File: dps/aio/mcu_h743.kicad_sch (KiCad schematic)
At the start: 65 parts, among them J301 TYPE-C 16P QTWT, J302 TF-021B-H265, J303 GPS WS-M181, J304 MTF-02P, U301 STM32H743VIH6, U302 SPL06-001 / DPS310, U303 BMI088, Y301 8MHz 12pF X32258MOB4SI

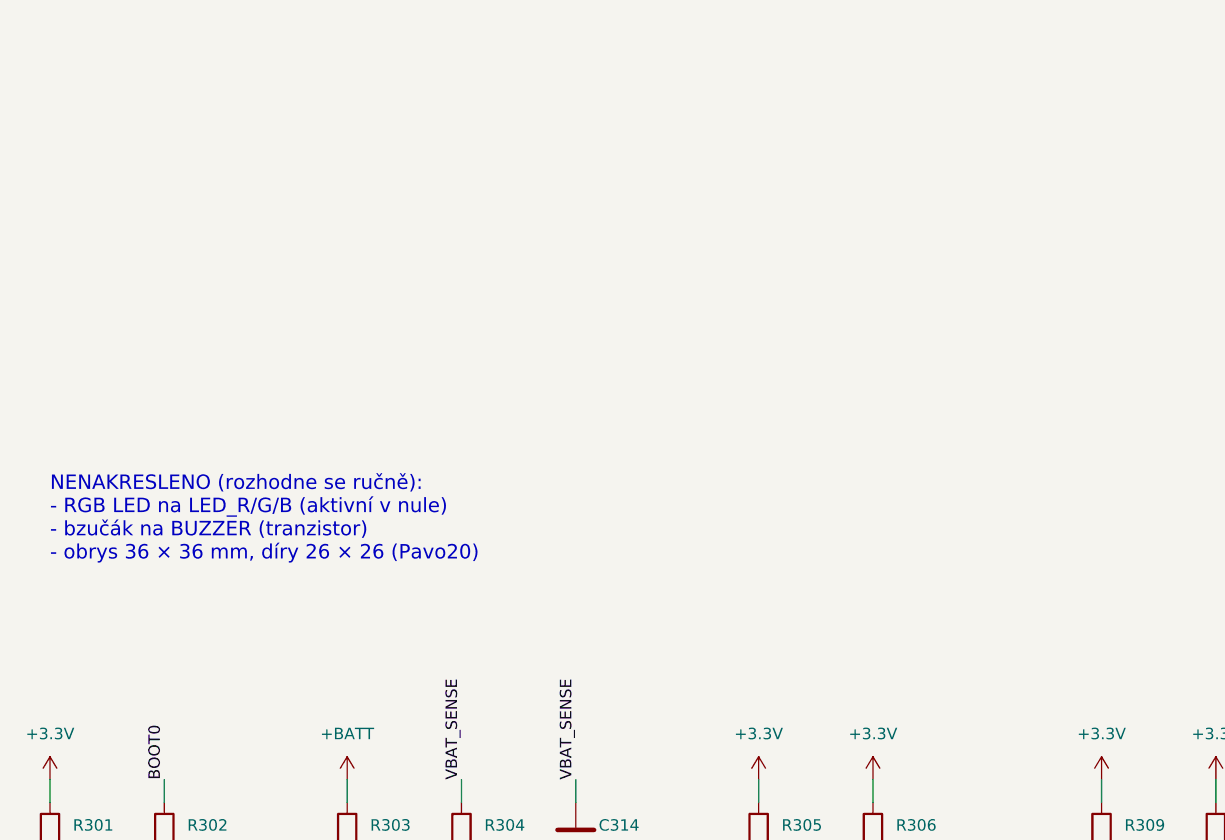
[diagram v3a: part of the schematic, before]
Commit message: feat: draw the AIO's RGB LED and buzzer switch, and keep the schematic generator in the repo
- D301-D303 XINGLIGHT XL-1005 0402 with anodes on 3.3 V: ArduPilot's
  GPIO_LED_RGB lights with a low (HAL_GPIO_LED_ON 0). Green and blue are
  OpenAIO's parts, red C965790 from the same series; 330R/150R/75R, ~3-5 mA.
- Q301 AO3400A low-side switch for an external active 5 V buzzer on pads
  BZ+/BZ- (BUZZ_ON_LVL 1), R319 holds it off through reset, D304 1N4148WS
  across the buzzer. A 2N7002 (Vgs(th) up to 2.5 V) would barely open at 3.3 V.
- dps/aio/gen/gen_aio.py writes every sheet with stable UUIDs; it now finds
  OpenAIO and KiCad's symbols on its own and only copies the board, rules,
  project and footprints when they are missing.
- NAVRH, README, web texts and tables follow; ERC still 18, explained.

Co-Authored-By: Claude Opus 5.5 <noreply@anthropic.com>
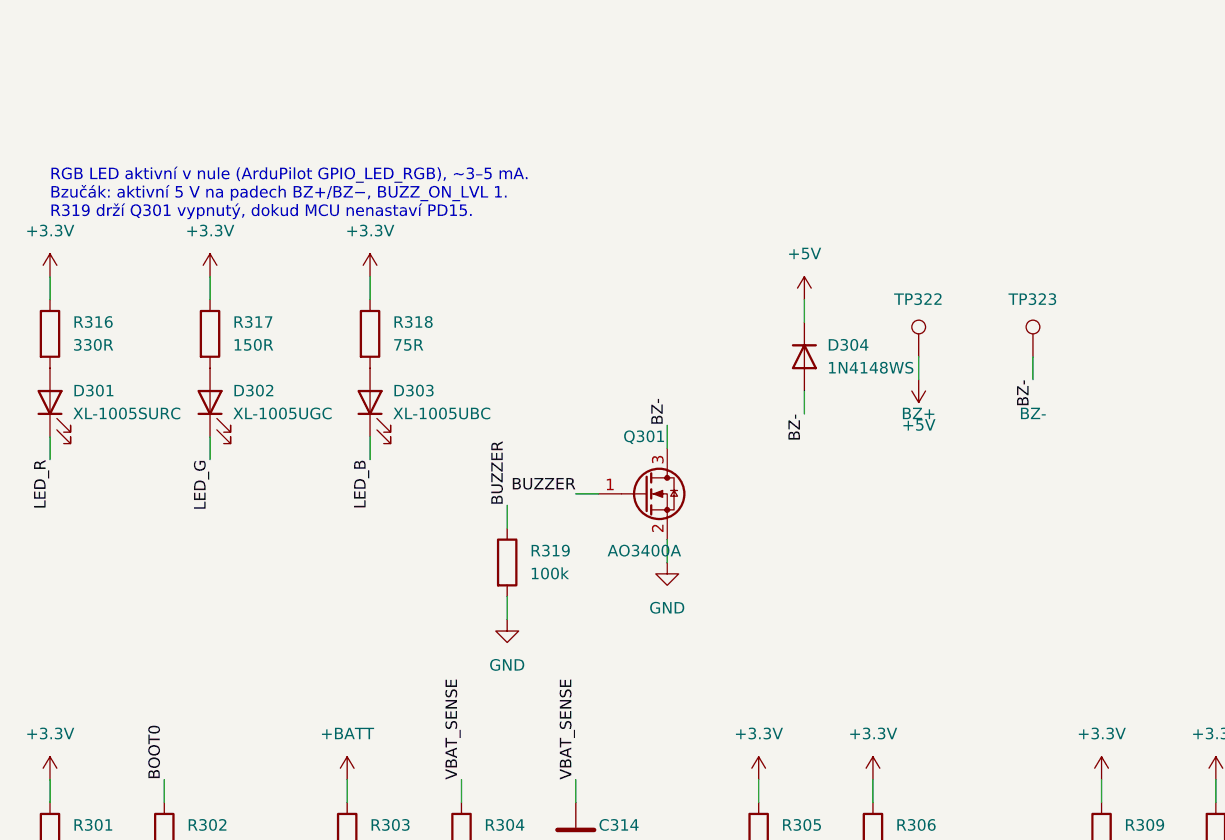
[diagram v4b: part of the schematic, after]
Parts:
- added D301: XL-1005SURC, lib:LED_0402_1005Metric, symbol lib:LED
- added D302: XL-1005UGC, lib:LED_0402_1005Metric, symbol lib:LED
- added D303: XL-1005UBC, lib:LED_0402_1005Metric, symbol lib:LED
- added D304: 1N4148WS, Diode_SMD:D_SOD-323, symbol Device:D
- added Q301: AO3400A, Package_TO_SOT_SMD:SOT-23, symbol Transistor_FET:Q_NMOS_GSD
- added R316: 330R, lib:R_0201_0603Metric, symbol lib:R
- added R317: 150R, lib:R_0201_0603Metric, symbol lib:R
- added R318: 75R, lib:R_0201_0603Metric, symbol lib:R
- added R319: 100k, lib:R_0201_0603Metric, symbol lib:R
- added TP322: BZ+, lib:TestPoint_Pad_D1.0mm, symbol lib:TestPoint
- added TP323: BZ-, lib:TestPoint_Pad_D1.0mm, symbol lib:TestPoint
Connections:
- net +3.3V: now also R316.1, R317.1, R318.1
- net +5V: now also D304.1 (K), TP322.1
- net BUZZER: now also Q301.1 (G), R319.1
- net GND: now also Q301.2 (S), R319.2
- net LED_B: now also D303.1 (K)
- net LED_G: now also D302.1 (K)
- net LED_R: now also D301.1 (K)
- new net: D303.2 (A), R318.2
- new net: D301.2 (A), R316.2
- new net: D302.2 (A), R317.2
- new net BZ-: D304.2 (A), Q301.3 (D), TP323.1
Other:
- note added: "RGB LED aktivní v nule (ArduPilot GPIO_LED_RGB), ~3–5 mA. Bzučák: aktivní 5 V na padech BZ+/BZ−, BUZZ_ON_LVL 1. R319 drží Q301 vypnutý, dokud MCU nenastaví PD15."
- note removed: "NENAKRESLENO (rozhodne se ručně): - RGB LED na LED_R/G/B (aktivní v nule) - bzučák na BUZZER (tranzistor) - obrys 36 × 36 mm, díry 26 × 26 (Pavo20)"

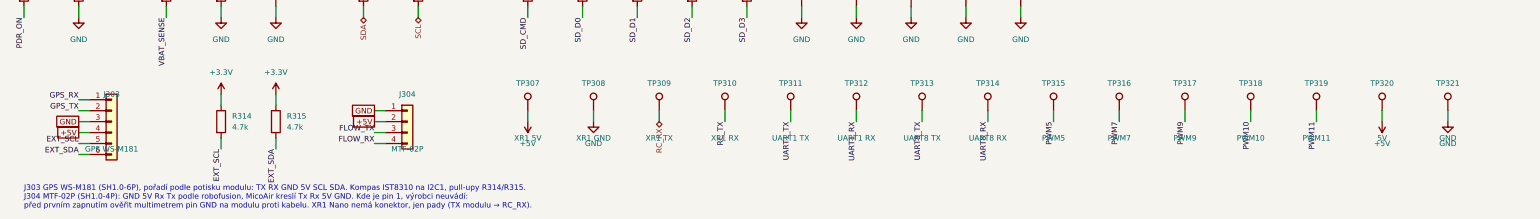
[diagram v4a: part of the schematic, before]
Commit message: feat: give the AIO MicoAir743-AIO's peripheral connectors
- J303 GPS (UART3 + I2C1), J304 UART4 and new J305 UART1 + UART6, SH1.0
  side entry, in MicoAir's order with pin 1 = GND (ArduPilot's README for the
  board puts pin 1 of the DJI connector at 12 V, the last row of its tables),
  so cables from a MicoAir fit. J305 replaces the XR1 and UART1 pads.
- The LD06 goes to pads (TP201 Tx, TP202 PWM, 5V/GND on TP320/TP321) as on
  MicoAir: the ZH1.5 connector needed 86 mm2 in one piece.
- Symbols and sheets now get UUIDs from their names, so adding or removing a
  part no longer shifts the others and breaks their link to the board.
- Placement: J304 fits on the back right edge as on MicoAir. J303 and J305 do
  not: every spot for a 6-pin SH (side 9.8 x 6.6 or vertical 9.8 x 5.2 mm)
  hits the ESC and power parts kept from OpenAIO, so they stay off the board.

Co-Authored-By: Claude Opus 5.5 <noreply@anthropic.com>
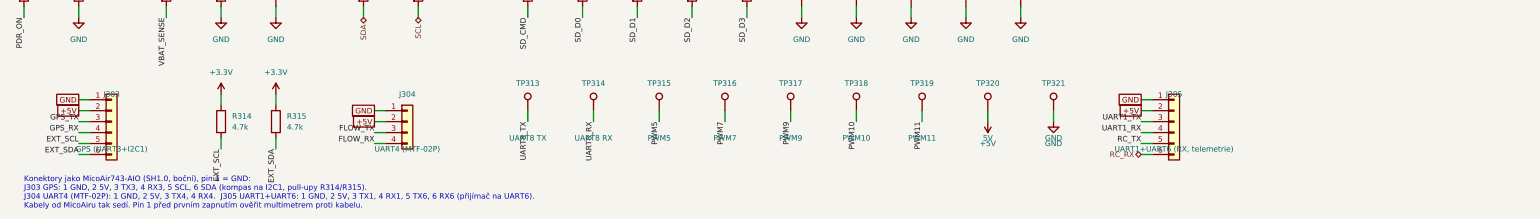
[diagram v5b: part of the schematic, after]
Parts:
- removed TP307: XR1 5V, lib:TestPoint_Pad_D1.0mm, symbol lib:TestPoint
- removed TP308: XR1 GND, lib:TestPoint_Pad_D1.0mm, symbol lib:TestPoint
- removed TP309: XR1 TX, lib:TestPoint_Pad_D1.0mm, symbol lib:TestPoint
- removed TP310: XR1 RX, lib:TestPoint_Pad_D1.0mm, symbol lib:TestPoint
- removed TP311: UART1 TX, lib:TestPoint_Pad_D1.0mm, symbol lib:TestPoint
- removed TP312: UART1 RX, lib:TestPoint_Pad_D1.0mm, symbol lib:TestPoint
- added J305: UART1+UART6 (RX, telemetrie), Connector_JST:JST_SH_SM06B-SRSS-TB_1x06-1MP_P1.00mm_Horizontal, symbol Connector_Generic:Conn_01x06
- J303: value GPS WS-M181 -> GPS (UART3+I2C1)
- J304: value MTF-02P -> UART4 (MTF-02P)
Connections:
- net +5V: now also J303.2 (Pin_2), J305.2 (Pin_2); no longer J303.4 (Pin_4)
- net GND: now also J303.1 (Pin_1), J305.1 (Pin_1); no longer J303.3 (Pin_3)
- net GPS_RX: now also J303.4 (Pin_4); no longer J303.1 (Pin_1)
- net GPS_TX: now also J303.3 (Pin_3); no longer J303.2 (Pin_2)
- net RC_RX: now also J305.6 (Pin_6)
- net RC_TX: now also J305.5 (Pin_5)
- net UART1_RX: now also J305.4 (Pin_4)
- net UART1_TX: now also J305.3 (Pin_3)
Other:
- note added: "Konektory jako MicoAir743-AIO (SH1.0, boční), pin 1 = GND: J303 GPS: 1 GND, 2 5V, 3 TX3, 4 RX3, 5 SCL, 6 SDA (kompas na I2C1, pull-upy R314/R315). J304 UART4 (MTF-02P): 1 GND, 2 5V, 3 TX4, 4 RX4. J305 UART1+UART6: 1 GND, 2 5V, 3 TX1, 4 RX1, 5 TX6, 6 RX6 (přijímač na UART6). Kabely od MicoAiru tak sedí. Pin 1 před prvním zapnutím ověřit multimetrem proti kabelu."
- note removed: "J303 GPS WS-M181 (SH1.0-6P), pořadí podle potisku modulu: TX RX GND 5V SCL SDA. Kompas IST8310 na I2C1, pull-upy R314/R315. J304 MTF-02P (SH1.0-4P): GND 5V Rx Tx podle robofusion, MicoAir kreslí Tx Rx 5V GND. Kde je pin 1, výrobci neuvádí: před prvním zapnutím ověřit multimetrem pin GND na modulu proti kabelu. XR1 Nano nemá konektor, jen pady (TX modulu → RC_RX)."

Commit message: feat: put all four MicoAir connectors on the AIO's edge and place it without the INA226
- The edge search found four spots no kept OpenAIO part blocks, so the ESCs
  stay as they are: J201 VTX front bottom, J303 GPS front right below motor 4,
  J305 UART1+UART6 back right, J304 UART4 back bottom. Motor pads are front
  only and the battery pads take the top edge, hence not MicoAir's places.
- Pads as on MicoAir: new lib:Pad_1.0x1.4mm (courtyard 1.2 x 1.6) instead of
  1 mm round test points with a 2 x 2 courtyard.
- Dropped for room, none of them on MicoAir: the VTX INA226 with its shunt,
  JP201 and the buzzer diode; Q301 is OpenAIO's AP1606 in DFN 1.0 x 0.6
  instead of an AO3400A in SOT-23. BATT2 defaults go; firmware rebuilt.
- Placement now treats pads, holes on both sides and the outer-layer copper
  of nets no new part uses (ESC inside, +BATT, the CSA+ via field) as
  obstacles, in 1 mm cells. vycisti_med.py removes the dangling RP2354
  leftovers and copper the new parts land on, never CSA+ or +BATT; the
  updater swaps changed footprints and sets sheet names.
- U303 (BMI088) and U201 (VTX buck) do not fit: no 3.3 x 3.3 mm is left on
  either side. DRC: 163 unconnected, otherwise OpenAIO's own warnings.

Co-Authored-By: Claude Opus 5.5 <noreply@anthropic.com>
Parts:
- removed D304: 1N4148WS, Diode_SMD:D_SOD-323, symbol Device:D
- Q301: value AO3400A -> AP1606; footprint Package_TO_SOT_SMD:SOT-23 -> lib:DFN-3L_L1.0-W0.6-P0.65-BR; symbol Transistor_FET:Q_NMOS_GSD -> lib:DMN1150UFB-7B; LCSC C20917 -> C2849580
- TP301, TP302, TP303, TP304, TP305, TP306, TP313, TP314, TP315, TP316, TP317, TP318, TP319, TP320, TP321, TP322, TP323: footprint lib:TestPoint_Pad_D1.0mm -> lib:Pad_1.0x1.4mm
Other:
- note added: "RGB LED aktivní v nule (ArduPilot GPIO_LED_RGB), ~3–5 mA. Bzučák: aktivní 5 V (piezo) na padech BZ+/BZ−, BUZZ_ON_LVL 1, bez diody jako MicoAir. R319 drží Q301 vypnutý, dokud MCU nenastaví PD15."
- note removed: "RGB LED aktivní v nule (ArduPilot GPIO_LED_RGB), ~3–5 mA. Bzučák: aktivní 5 V na padech BZ+/BZ−, BUZZ_ON_LVL 1. R319 drží Q301 vypnutý, dokud MCU nenastaví PD15."

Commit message: feat: fit every AIO part on the board: switch the VTX off +10V and take an ICM-42688-P as the second IMU
The VTX buck and the BMI088 did not fit; the largest free spot was 2.5 x 2.9 mm.
The VTX now hangs on fc_power's +10V behind a TPS22810 load switch (as OpenAIO
feeds it, but switchable), and the second IMU is an ICM-42688-P on OpenAIO's
LGA-14 footprint. The board update now also carries values and LCSC numbers.

Co-Authored-By: Claude Opus 5.5 <noreply@anthropic.com>
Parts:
- added C324: 10n, lib:C_0201_0603Metric, symbol lib:C
- C319: value 100n -> 2.2uF; LCSC C76939 -> (none)
- U303: value BMI088 -> ICM-42688-P; footprint Package_LGA:Bosch_LGA-16_4.5x3mm_P0.5mm_LayoutBorder7x1y_ClockwisePinNumbering -> lib:LGA-14_L3.0-W2.5-P0.50-BR; symbol Sensor_Motion:BMI088 -> lib:LSM6DSV16XTR
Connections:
- net +3.3V: now also U303.5 (Vdd_IO), U303.8 (Vdd), C324.1; no longer U303.11 (VDDIO), U303.3 (VDD)
- net GND: now also U303.10 (OCS_Aux), U303.11 (SDO_Aux), U303.3 (SCx/AH2/Qvar2), U303.9 (INT2), C324.2; no longer U303.4 (GNDA)
- net IMU2_MISO: now also U303.1 (SDO/SA0); no longer U303.10 (SDO2), U303.15 (SDO1)
- net IMU2_MOSI: now also U303.14 (SDA); no longer U303.9 (SDI/SDA)
- net IMU2_SCK: now also U303.13 (SCL); no longer U303.8 (SCK/SCL)
- net IMU2_ACC_CS renamed IMU2_CS
- net IMU2_CS: now also U303.12 (CS); no longer U303.14 (~{CSB1})
- net IMU2_ACC_INT renamed IMU2_INT
- net IMU2_INT: now also U303.4 (INT1); no longer U303.16 (INT1)
- net IMU2_GYR_CS: no longer names the net of U301.B6 (PD5)
- net IMU2_GYR_CS: no longer U303.5 (~{CSB2})
- net IMU2_GYR_INT: no longer names the net of U301.B1 (PC15)
- net IMU2_GYR_INT: no longer U303.12 (INT3)
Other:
- note added: "U303 ICM-42688-P na SPI2 (MicoAir tu má BMI088, 4,5 × 3 mm se nevešel). Pouzdro LGA-14 2,5 × 3 jako BMI270. INT1 = data ready, RESV a FSYNC na GND. VDD 100 nF + 2,2 µF (C318, C319), VDDIO 10 nF (C324) podle DS-000347."
- note removed: "U303 BMI088 jako MicoAir: SPI2, PS = GND (SPI), SDO1+SDO2 = MISO, INT1 = data ready akcel., INT3 = gyro."
- moved on the sheet: C317

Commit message: feat: route the AIO with its own router after laying it out like MicoAir
The peripherals sat where OpenAIO put them for the RP2354, so about 20 signals
left the H743's BGA on the wrong side. The connectors now sit as on MicoAir,
mirrored, and GPS, receiver, LD06 and both IMUs move to pins whose balls face
them; SERIAL_ORDER keeps the SERIALn numbers. New scripts escape the BGA, clear
OpenAIO leftovers, route in several passes, stitch GND islands and place the
USB-C D+/D- jumpers. 134 of 156 pairs are routed, 22 remain, DRC is clean.

Co-Authored-By: Claude Opus 5.5 <noreply@anthropic.com>
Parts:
- J303: value GPS (UART3+I2C1) -> GPS (SERIAL3+I2C1)
- J305: value UART1+UART6 (RX, telemetrie) -> SERIAL1+SERIAL6 (RX, telemetrie)
- TP313: value UART8 TX -> UART7 TX
- TP314: value UART8 RX -> UART7 RX
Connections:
- net UART5_TX is gone; now on net RC_TX: U301.B5 (PB6)
- net GPS_RX: now also U301.D4 (PE0); no longer U301.J9 (PD9)
- net GPS_TX: now also U301.C4 (PE1); no longer U301.K9 (PD8)
- net IMU2_CS: now also U301.K8 (PB12); no longer U301.D7 (PD4)
- net IMU2_INT: now also U301.J6 (PE12); no longer U301.A1 (PC14)
- net IMU2_SCK: now also U301.J8 (PB13); no longer U301.C7 (PD3)
- net IMU_CS: now also U301.G3 (PA4); no longer U301.A8 (PA15)
- net IMU_INT: now also U301.G4 (PC4); no longer U301.A5 (PB7)
- net IMU_SPI.MISO: now also U301.J3 (PA6); no longer U301.A6 (PB4)
- net IMU_SPI.MOSI: now also U301.K3 (PA7); no longer U301.C6 (PD6)
- net IMU_SPI.SCK: now also U301.H3 (PA5); no longer U301.A7 (PB3)
- net LIDAR_TX: now also U301.J9 (PD9); no longer U301.C5 (PB5)
- net RC_RX: now also U301.C5 (PB5); no longer U301.E10 (PC7)
- net RC_TX: no longer U301.F10 (PC6)
- net UART7_RX: now also TP314.1
- net UART7_TX: now also TP313.1
- removed net UART8_RX: TP314.1, U301.D4 (PE0)
- removed net UART8_TX: TP313.1, U301.C4 (PE1)
- new net UART3_TX: U301.K9 (PD8)
- no-connect marks 25 -> 27
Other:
- note added: "Konektory jako MicoAir743-AIO (SH1.0, boční), pin 1 = GND: J303 GPS: 1 GND, 2 5V, 3 TX, 4 RX (UART8 = SERIAL3), 5 SCL, 6 SDA (kompas na I2C1, pull-upy R314/R315). J304 UART4 (MTF-02P): 1 GND, 2 5V, 3 TX4, 4 RX4. J305: 1 GND, 2 5V, 3 TX1, 4 RX1 (USART1 = SERIAL1), 5 TX, 6 RX (přijímač, UART5 = SERIAL6). GPS a přijímač jsou na UARTech, jejichž kuličky míří ke konektorům (obvod desky je zrcadlo Mico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"
- note removed: "Konektory jako MicoAir743-AIO (SH1.0, boční), pin 1 = GND: J303 GPS: 1 GND, 2 5V, 3 TX3, 4 RX3, 5 SCL, 6 SDA (kompas na I2C1, pull-upy R314/R315). J304 UART4 (MTF-02P): 1 GND, 2 5V, 3 TX4, 4 RX4. J305 UART1+UART6: 1 GND, 2 5V, 3 TX1, 4 RX1, 5 TX6, 6 RX6 (přijímač na UART6). Kabely od MicoAiru tak sedí. Pin 1 před prvním zapnutím ověřit multimetrem proti kabelu."
